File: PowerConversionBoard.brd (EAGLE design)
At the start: 152.4 x 101.6 mm, 48 parts, among them U1 LM2678, U2 LM2678

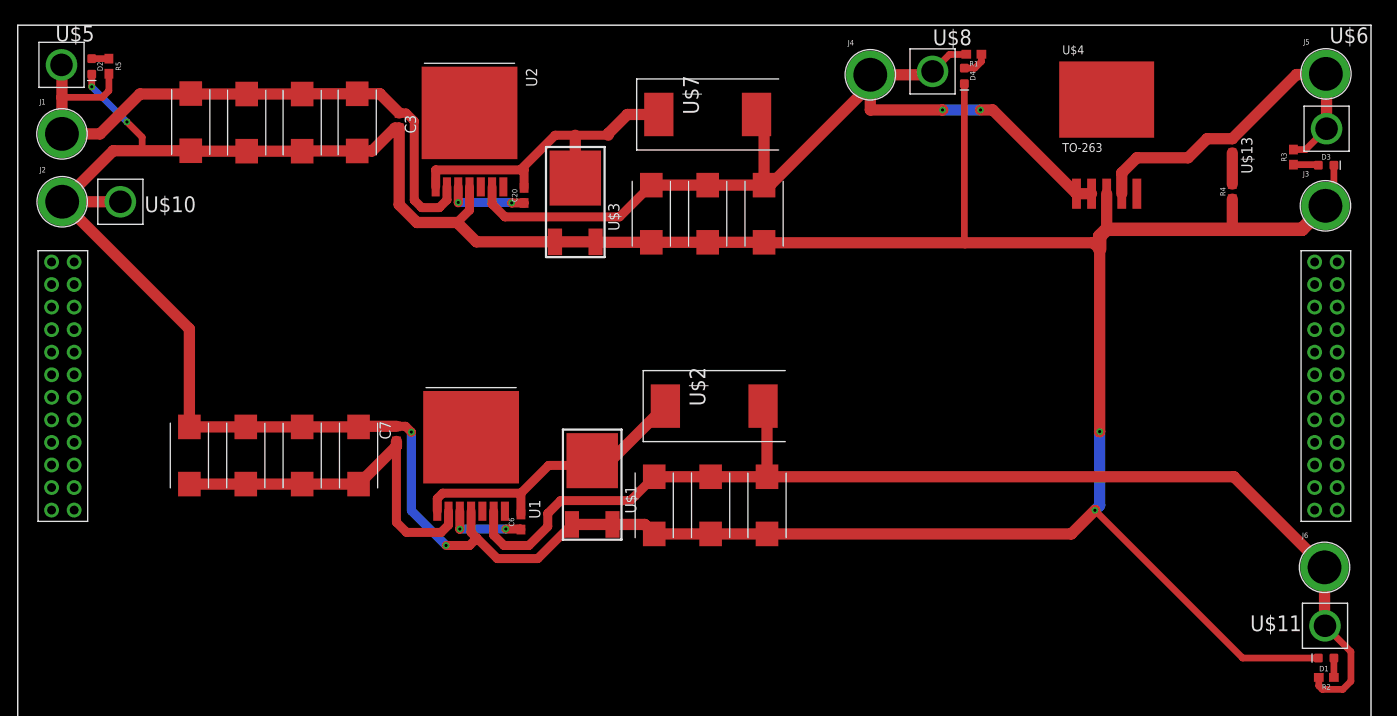
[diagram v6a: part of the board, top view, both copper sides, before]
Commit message: power plane
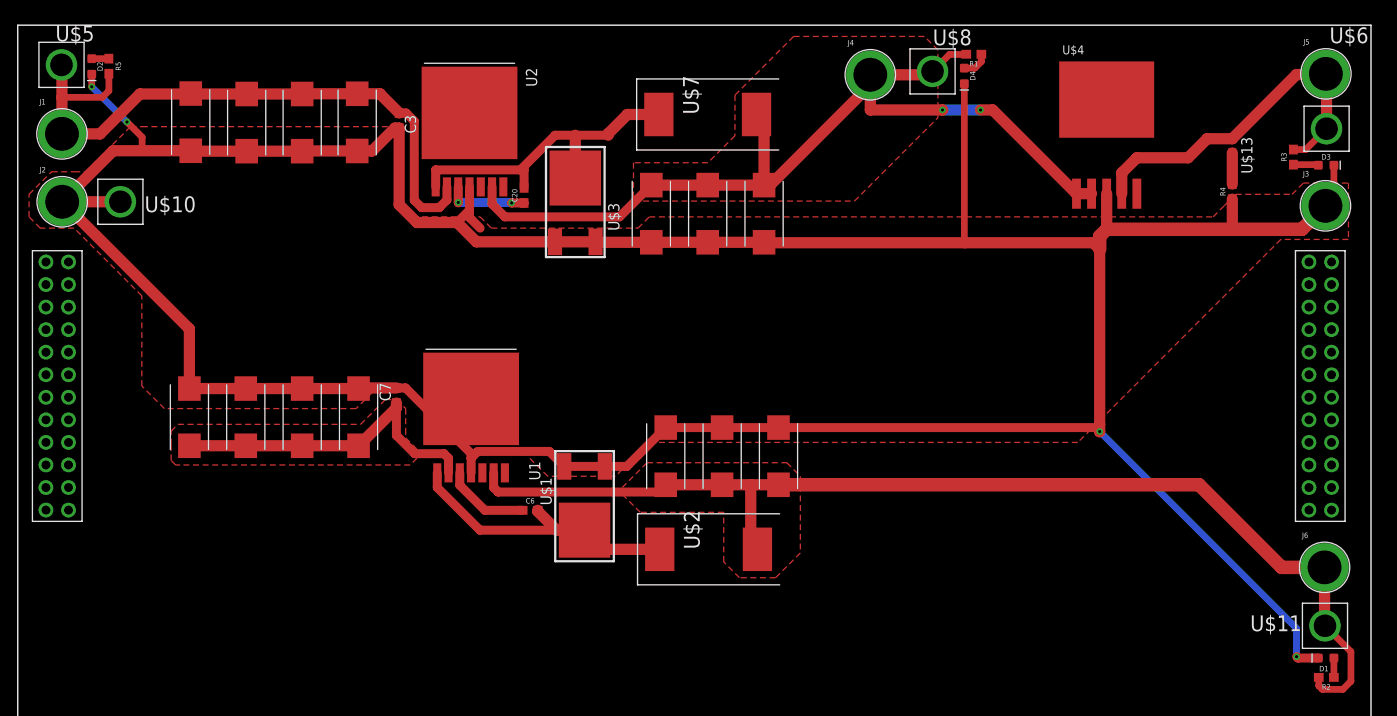
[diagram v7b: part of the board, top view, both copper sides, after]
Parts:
- U$9: device Dist_to_Conversion_Connector:CONVERSION_TSW_12X2 -> Conversion_Connector:CONVERSION_TSW_12X2
- moved U$2 16.1 mm to (77.8, 42.6)
- moved C12 15.1 mm to (85.7, 53.1), turned to 90 degrees
- moved C11 12.7 mm to (73.0, 53.1), turned to 90 degrees
- moved C10 5.69 mm to (79.3, 53.1), turned to 90 degrees
- moved C15 4.32 mm to (19.3, 57.5)
- moved C16 4.32 mm to (25.7, 57.5)
- moved C17 4.32 mm to (32.0, 57.5)
- moved C18 4.32 mm to (38.4, 57.5)
- moved C7 4.32 mm to (42.6, 59.9)
- moved U1 4.32 mm to (51.1, 59.5)
- moved U$1 1.84 mm to (63.8, 47.8), turned to 90 degrees
- moved C6 1.68 mm to (57.7, 47.0), turned to 0 degrees
- moved U$9 0.64 mm to (3.17, 74.9)
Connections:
- new net CAN_H: U$9.47
- new net CAN_L: U$9.48
- net +12V: now also U$9.1, U$9.10, U$9.11, U$9.12, U$9.2, U$9.3, U$9.4, U$9.5, U$9.6, U$9.7, U$9.8, U$9.9
- net +3.3V: now also U$9.25, U$9.26, U$9.27, U$9.28, U$9.29, U$9.30, U$9.31, U$9.32
- net GND: now also U$9.13, U$9.14, U$9.15, U$9.16, U$9.17, U$9.18, U$9.19, U$9.20, U$9.21, U$9.22, U$9.23, U$9.24, U$9.33, U$9.34, U$9.35, U$9.36, U$9.37, U$9.38, U$9.39, U$9.40, U$9.41
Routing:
- net GND: track 427.1 -> 411.0 mm, vias 6 -> 4
- net +5V: track 132.4 -> 127.2 mm
- net N$20: track 43.0 -> 37.9 mm
- net N$3: track 9.04 -> 9.64 mm, vias 2 -> 0
- added copper zone on layer 1, net +5V
- added copper zone on layer 1, net +5V_3.3V
- added copper zone on layer 1, net GND
- added copper zone on layer 1, net N$20

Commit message: plane ez
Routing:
- net GND: track 411.0 -> 408.9 mm
- added copper zone on layer 1, net +12V
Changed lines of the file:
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@@
 <setting verticaltext="up"/>
 </settings>
-<grid distance="50" unitdist="mil" unit="mil" style="lines" multiple="1" display="yes" altdistance="5" altunitdist="mil" altunit="inch"/>
+<grid distance="10" unitdist="mil" unit="mil" style="lines" multiple="1" display="yes" altdistance="5" altunitdist="mil" altunit="inch"/>
 <layers>
 <layer number="1" name="Top" color="4" fill="1" visible="yes" active="yes"/>
@@
 <contactref element="U$9" pad="8"/>
 <contactref element="U$9" pad="10"/>
-<wire x1="5.715" y1="74.93" x2="4.9784" y2="89.3572" width="0" layer="19" extent="1-1"/>
+<polygon width="0.254" layer="1">
+<vertex x="2.286" y="86.868"/>
+<vertex x="7.366" y="86.868"/>
+<vertex x="13.716" y="93.218"/>
+<vertex x="16.51" y="93.218"/>
+<vertex x="17.78" y="91.948"/>
+<vertex x="41.91" y="91.948"/>
+<vertex x="42.672" y="91.186"/>
+<vertex x="43.434" y="91.186"/>
+<vertex x="43.434" y="93.472"/>
+<vertex x="41.402" y="95.504"/>
+<vertex x="41.148" y="95.758"/>
+<vertex x="10.16" y="95.758"/>
+<vertex x="9.906" y="95.504"/>
+<vertex x="9.652" y="95.25"/>
+<vertex x="9.652" y="94.234"/>
+<vertex x="8.89" y="93.472"/>
+<vertex x="8.128" y="93.472"/>
+<vertex x="7.62" y="93.98"/>
+<vertex x="7.112" y="94.488"/>
+<vertex x="7.112" y="99.06"/>
+<vertex x="5.842" y="100.33"/>
+<vertex x="3.81" y="100.33"/>
+<vertex x="2.286" y="98.806"/>
+</polygon>
 <wire x1="5.715" y1="72.39" x2="5.715" y2="74.93" width="0" layer="19" extent="1-1"/>
 <wire x1="3.175" y1="74.93" x2="5.715" y2="74.93" width="0" layer="19" extent="1-1"/>
@@
 <wire x1="3.175" y1="64.77" x2="5.715" y2="64.77" width="0" layer="19" extent="1-1"/>
 <wire x1="3.175" y1="62.23" x2="5.715" y2="62.23" width="0" layer="19" extent="1-1"/>
+<wire x1="4.9784" y1="89.3572" x2="5.715" y2="74.93" width="0" layer="19" extent="1-1"/>
 </signal>
 <signal name="GND">
@@
 <wire x1="19.3294625" y1="67.3861375" x2="19.3294" y2="60.6748" width="1.27" layer="1"/>
 <wire x1="43.0784" y1="89.8788" x2="42.9514" y2="90.0058" width="1.016" layer="1"/>
-<wire x1="50.8762" y1="83.3882" x2="50.8762" y2="80.772" width="1.016" layer="1"/>
-<wire x1="42.9514" y1="90.0058" x2="42.9514" y2="81.3816" width="1.27" layer="1"/>
-<wire x1="44.958" y1="79.375" x2="42.9514" y2="81.3816" width="1.27" layer="1"/>
+<wire x1="42.9514" y1="81.3816" x2="44.958" y2="79.375" width="1.27" layer="1"/>
 <wire x1="49.4792" y1="79.375" x2="44.958" y2="79.375" width="1.27" layer="1"/>
-<wire x1="50.8762" y1="80.772" x2="49.4792" y2="79.375" width="1.016" layer="1"/>
 <wire x1="10.75" y1="87.458" x2="5.0038" y2="81.7118" width="1.27" layer="1"/>
 <wire x1="19.4818" y1="87.458" x2="10.75" y2="87.458" width="1.27" layer="1"/>
@@
 <vertex x="1.27" y="80.01"/>
 </polygon>
-<wire x1="50.8762" y1="80.772" x2="50.8762" y2="79.9338" width="1.016" layer="1"/>
-<wire x1="50.8762" y1="79.9338" x2="52.07" y2="78.74" width="1.016" layer="1"/>
+<wire x1="42.9514" y1="90.0058" x2="42.9514" y2="82.296" width="1.27" layer="1"/>
+<wire x1="42.9514" y1="82.296" x2="42.9514" y2="81.3816" width="1.27" layer="1"/>
+<wire x1="50.8762" y1="83.3882" x2="50.8762" y2="80.0862" width="1.016" layer="1"/>
+<wire x1="50.8762" y1="80.0862" x2="50.8" y2="80.01" width="1.016" layer="1"/>
+<wire x1="50.8" y1="80.01" x2="50.165" y2="79.375" width="1.016" layer="1"/>
+<wire x1="50.165" y1="79.375" x2="49.4792" y2="79.375" width="1.016" layer="1"/>
 <wire x1="122.6312" y1="82.6196" x2="122.6312" y2="93.2196" width="0" layer="19" extent="1-1"/>
-<wire x1="50.8762" y1="91.7194" x2="43.0784" y2="89.8788" width="0" layer="19" extent="1-1"/>
+<wire x1="14.0081" y1="87.5411" x2="19.4818" y2="87.458" width="0" layer="19" extent="1-1"/>
+<wire x1="42.9514" y1="82.296" x2="50.8762" y2="91.7194" width="0" layer="19" extent="1-1"/>
+<wire x1="51.054" y1="59.5122" x2="51.054" y2="51.181" width="0" layer="19" extent="1-1"/>
 <wire x1="5.715" y1="59.69" x2="19.3294" y2="60.6748" width="0" layer="19" extent="1-1"/>
 <wire x1="5.715" y1="57.15" x2="5.715" y2="59.69" width="0" layer="19" extent="1-1"/>
